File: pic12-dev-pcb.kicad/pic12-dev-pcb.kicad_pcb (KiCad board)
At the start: 2 copper layers, 25.4 x 40.1 mm, 12 parts, among them J1 PGM-Conn, J2 App-Conn1, J3 App-Conn2, J4 Conn_SR, J6 Conn_BB1, U1 PIC12F675-ISN

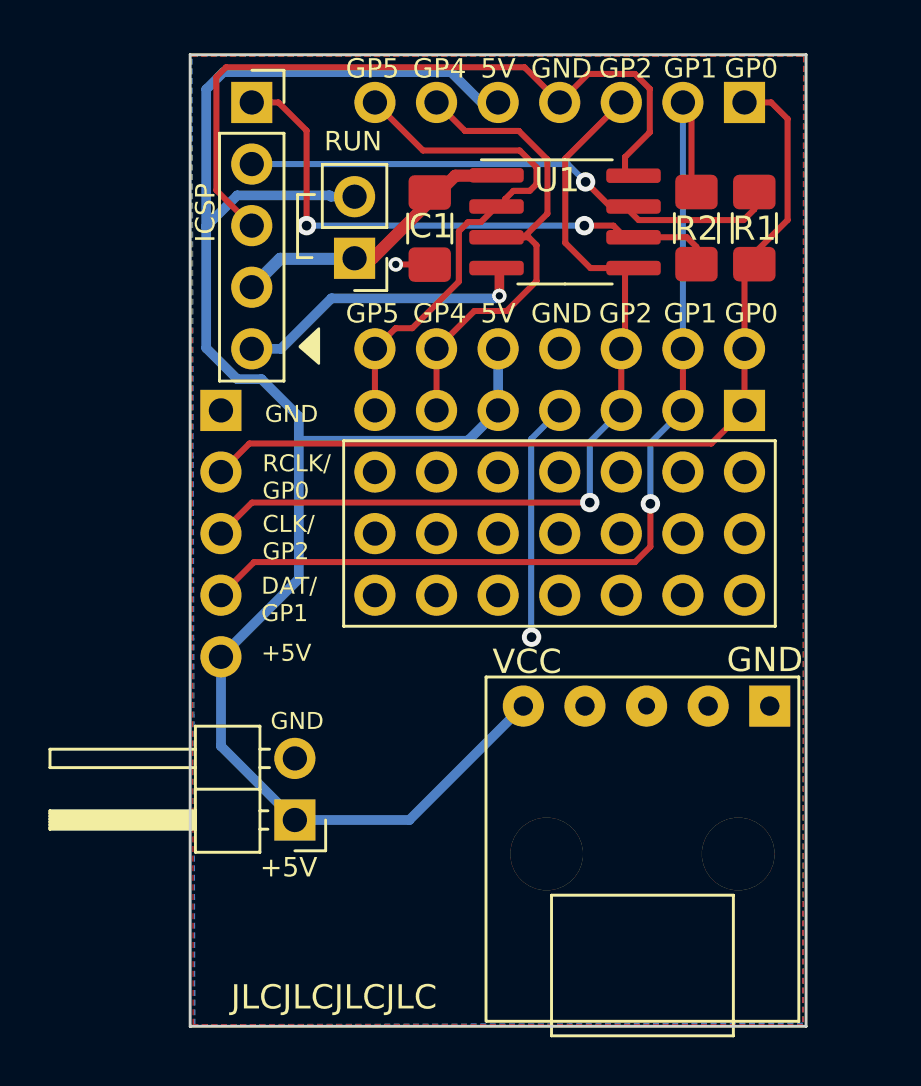
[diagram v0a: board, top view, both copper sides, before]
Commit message: Rev5: added GP3 to connectors
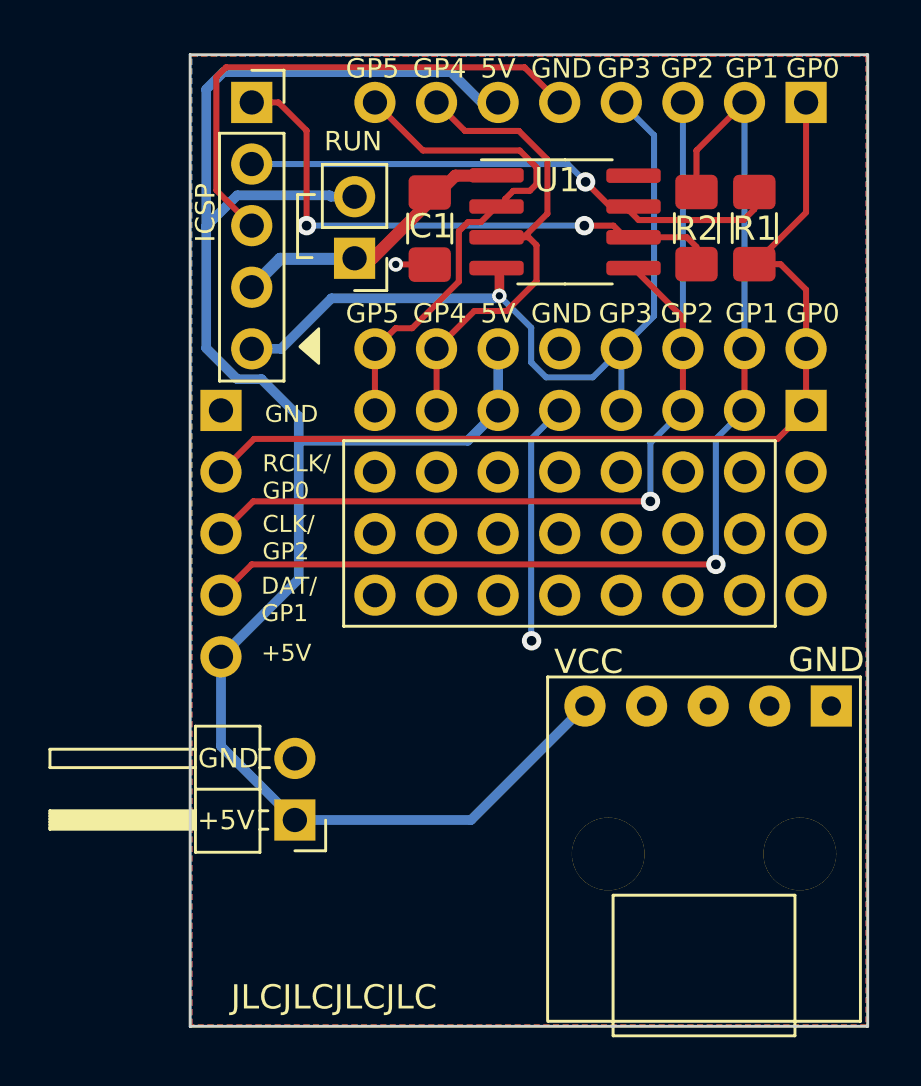
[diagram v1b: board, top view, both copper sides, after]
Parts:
- removed the REF** at (104.1, 91.4)
- added REF**: Proto_Area_08x03_P2.54mm_Drill1.0mm, Proto_Area:Proto_Area_08x03, F.Cu at (104.1, 91.4)
- J2: footprint Connector_PinHeader_2.54mm:PinHeader_1x07_P2.54mm_Vertical -> Connector_PinHeader_2.54mm:PinHeader_1x08_P2.54mm_Vertical
- J3: footprint Connector_PinHeader_2.54mm:PinHeader_2x07_P2.54mm_Vertical -> Connector_PinHeader_2.54mm:PinHeader_2x08_P2.54mm_Vertical
- moved J2 2.54 mm to (121.9, 76.2)
- moved J3 2.54 mm to (121.9, 88.9)
- moved USB1 2.54 mm to (123.0, 101.1)
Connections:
- J1 pad 5: Net-(J1-Pad5) -> /GP3
- J2 pad 4: GND -> /GP3
- J2 pad 5: /+5V -> GND
- J2 pad 6: /GP4 -> /+5V
- J2 pad 7: /GP5 -> /GP4
- J3 pad 10: /+5V -> GND
- J3 pad 11: /GP4 -> /+5V
- J3 pad 12: /GP4 -> /+5V
- J3 pad 13: /GP5 -> /GP4
- J3 pad 14: /GP5 -> /GP4
- J3 pad 7: GND -> /GP3
- J3 pad 8: GND -> /GP3
- J3 pad 9: /+5V -> GND
- U1 pad 4: Net-(J1-Pad5) -> /GP3
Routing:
- net /GP3: track 0.00 -> 33.9 mm, vias 0 -> 1
- net Net-(J1-Pad5): track 12.3 -> 0.00 mm, vias 1 -> 0
- net GND: track 41.5 -> 33.0 mm
- net /GP2: track 35.7 -> 39.5 mm
- net /GP1: track 41.3 -> 45.0 mm
- net /GP0: track 37.7 -> 41.3 mm
- net /+5V: track 77.6 -> 80.1 mm
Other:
- board size 25.4 x 40.1 mm -> 27.9 x 40.1 mm
- board text added: "GP3"
- board text added: "Rev 5"
- board text removed: "Rev 4"

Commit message: Rev6: added LEDs and button
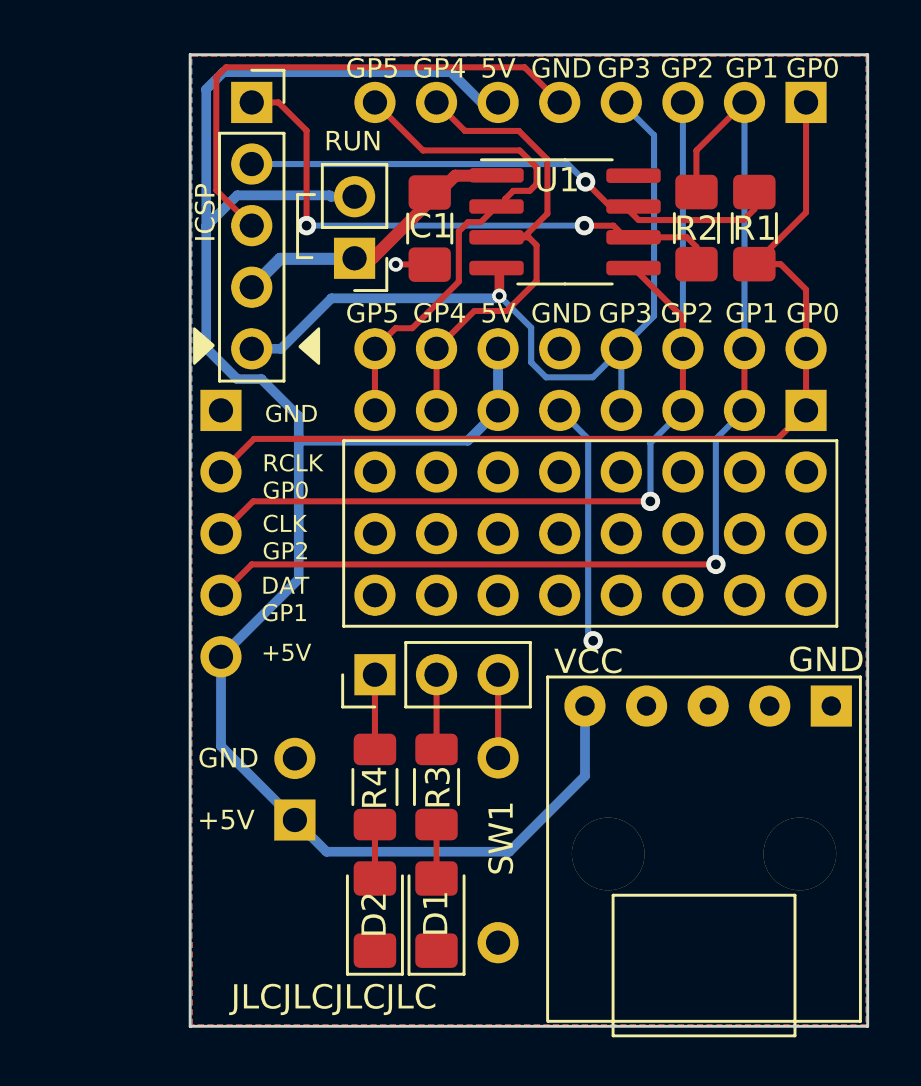
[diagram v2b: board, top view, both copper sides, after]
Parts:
- added D1: LED, LED_SMD:LED_1206_3216Metric_Pad1.42x1.75mm_HandSolder, F.Cu at (106.7, 109.7)
- added D2: LED, LED_SMD:LED_1206_3216Metric_Pad1.42x1.75mm_HandSolder, F.Cu at (104.1, 109.7)
- added J5: Conn_01x03_Male, Connector_PinHeader_2.54mm:PinHeader_1x03_P2.54mm_Vertical, F.Cu at (104.1, 99.8)
- added R3: 1kΩ, Resistor_SMD:R_1206_3216Metric_Pad1.30x1.75mm_HandSolder, F.Cu at (106.7, 104.4)
- added R4: 1kΩ, Resistor_SMD:R_1206_3216Metric_Pad1.30x1.75mm_HandSolder, F.Cu at (104.1, 104.4)
- added SW1: SW_Push, user:SW_PUSH_SLIM_1x4, F.Cu at (109.2, 103.2)
- J6: footprint Connector_PinHeader_2.54mm:PinHeader_1x02_P2.54mm_Horizontal -> Connector_PinHeader_2.54mm:PinHeader_1x02_P2.54mm_Vertical; moved to B.Cu
- turned J6 to 0 degrees
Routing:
- net Net-(J5-Pad3): track 0.00 -> 3.43 mm
- net Net-(J5-Pad2): track 0.00 -> 3.08 mm
- net Net-(J5-Pad1): track 0.00 -> 3.08 mm
- net /+5V: track 80.1 -> 82.9 mm
- net Net-(D2-Pad2): track 0.00 -> 2.22 mm
- net Net-(D1-Pad2): track 0.00 -> 2.22 mm
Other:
- rule pad_to_mask_clearance: 0.051 -> 0
- board text added: "CLK GP2"
- board text added: "DAT GP1"
- board text added: "RCLK GP0"
- board text added: "Rev 6"
- board text removed: "CLK/ GP2"
- board text removed: "DAT/ GP1"
- board text removed: "RCLK/ GP0"
- board text removed: "Rev 5"
